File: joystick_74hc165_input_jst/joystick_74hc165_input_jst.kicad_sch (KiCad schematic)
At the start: 38 parts, among them J11 Conn_01x05, J12 Conn_01x02, J13 Conn_01x02, J14 Conn_01x02, J15 Conn_01x02, J16 Conn_01x02, J17 Conn_01x02, J18 Conn_01x02, J19 Conn_01x02, J21 Conn_01x05, J22 Conn_01x02, J23 Conn_01x02, J24 Conn_01x02, J25 Conn_01x02, J26 Conn_01x02, J27 Conn_01x02, J28 Conn_01x02, J29 Conn_01x02

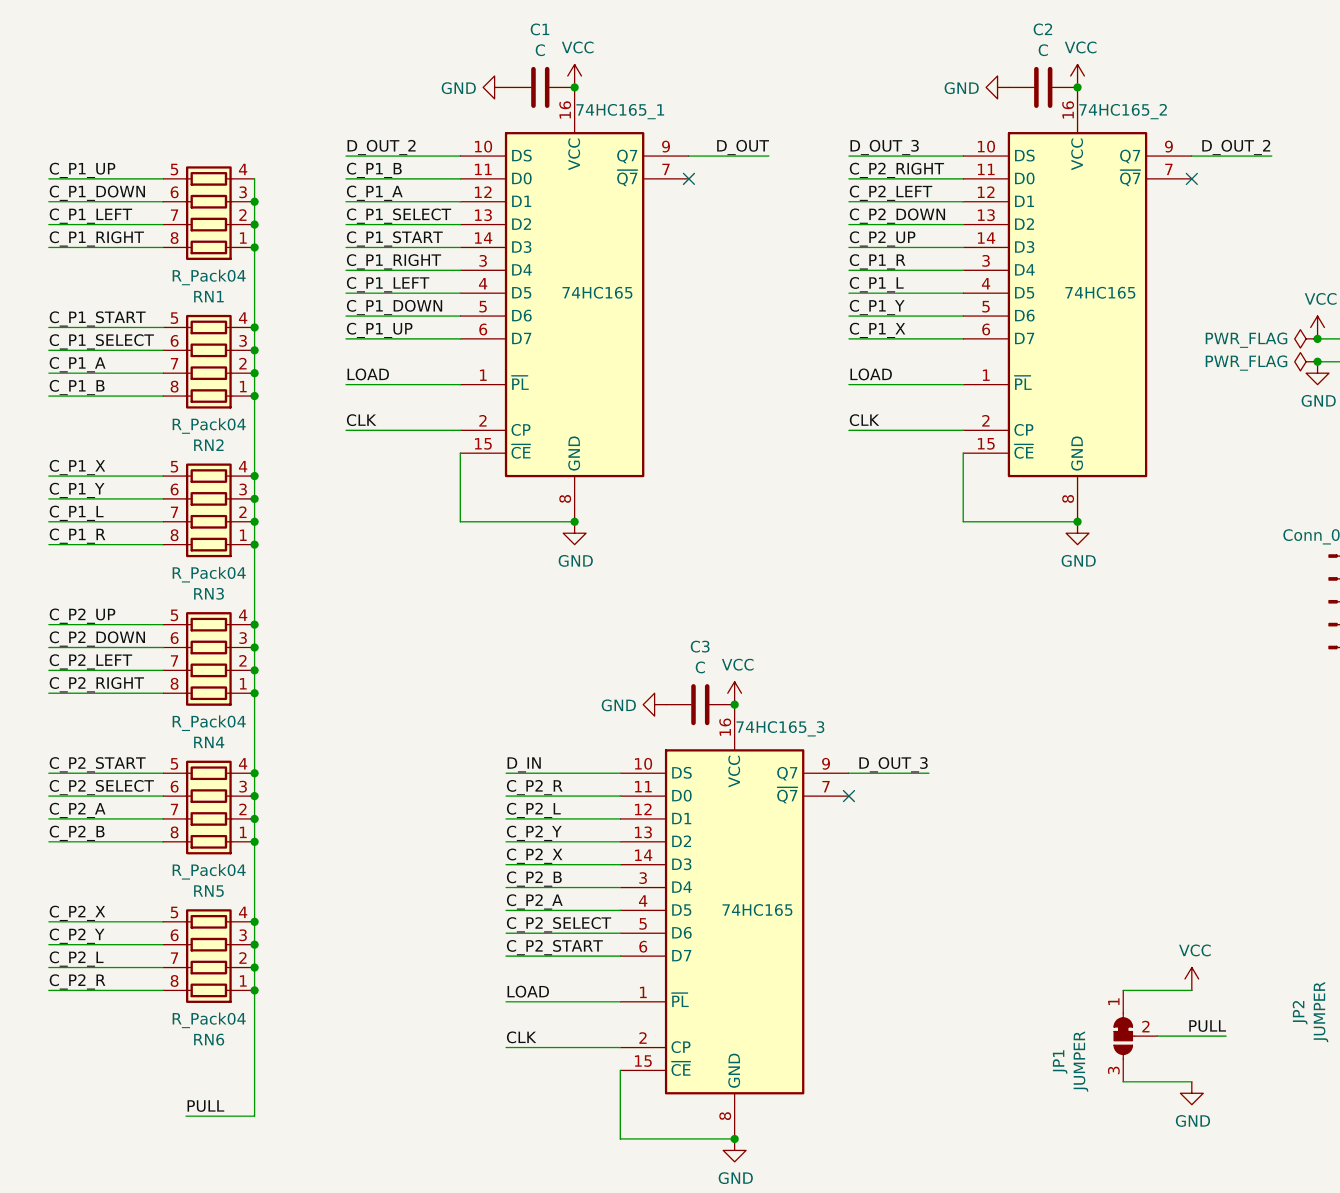
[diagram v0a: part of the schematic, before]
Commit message: 부품 값 입력
Signed-off-by: Ju, Gyeong-min <jcmh74@gmail.com>
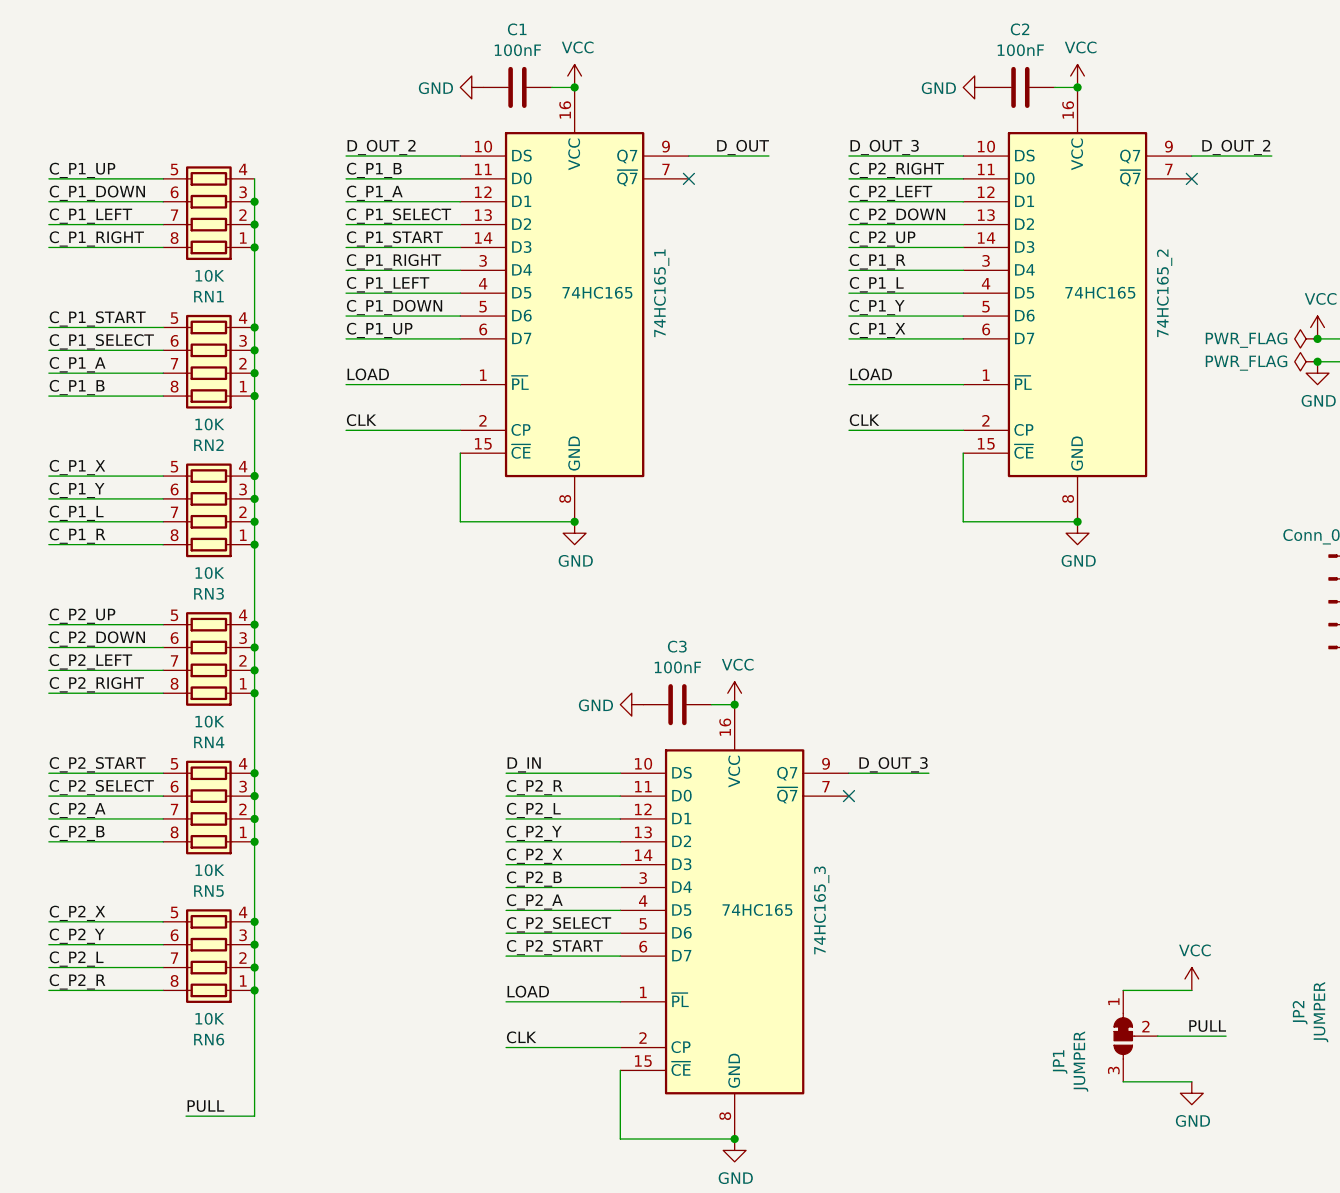
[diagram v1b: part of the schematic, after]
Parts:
- C1, C2, C3: value C -> 100nF
- RN1, RN2, RN3, RN4, RN5, RN6: value R_Pack04 -> 10K
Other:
- moved on the sheet: C1, C2, C3
